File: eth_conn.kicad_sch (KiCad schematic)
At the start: 36 parts, among them T1 H1102NLT, U27 ESDS304DBVR, U3 CD-HD01, U4 CD-HD01

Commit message: did a bit of placement
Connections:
- net MDI.RX-: now also U27.3; no longer U27.5
- net MDI.TX+: now also U27.1; no longer U27.3
- net MDI.TX-: now also U27.5; no longer U27.1

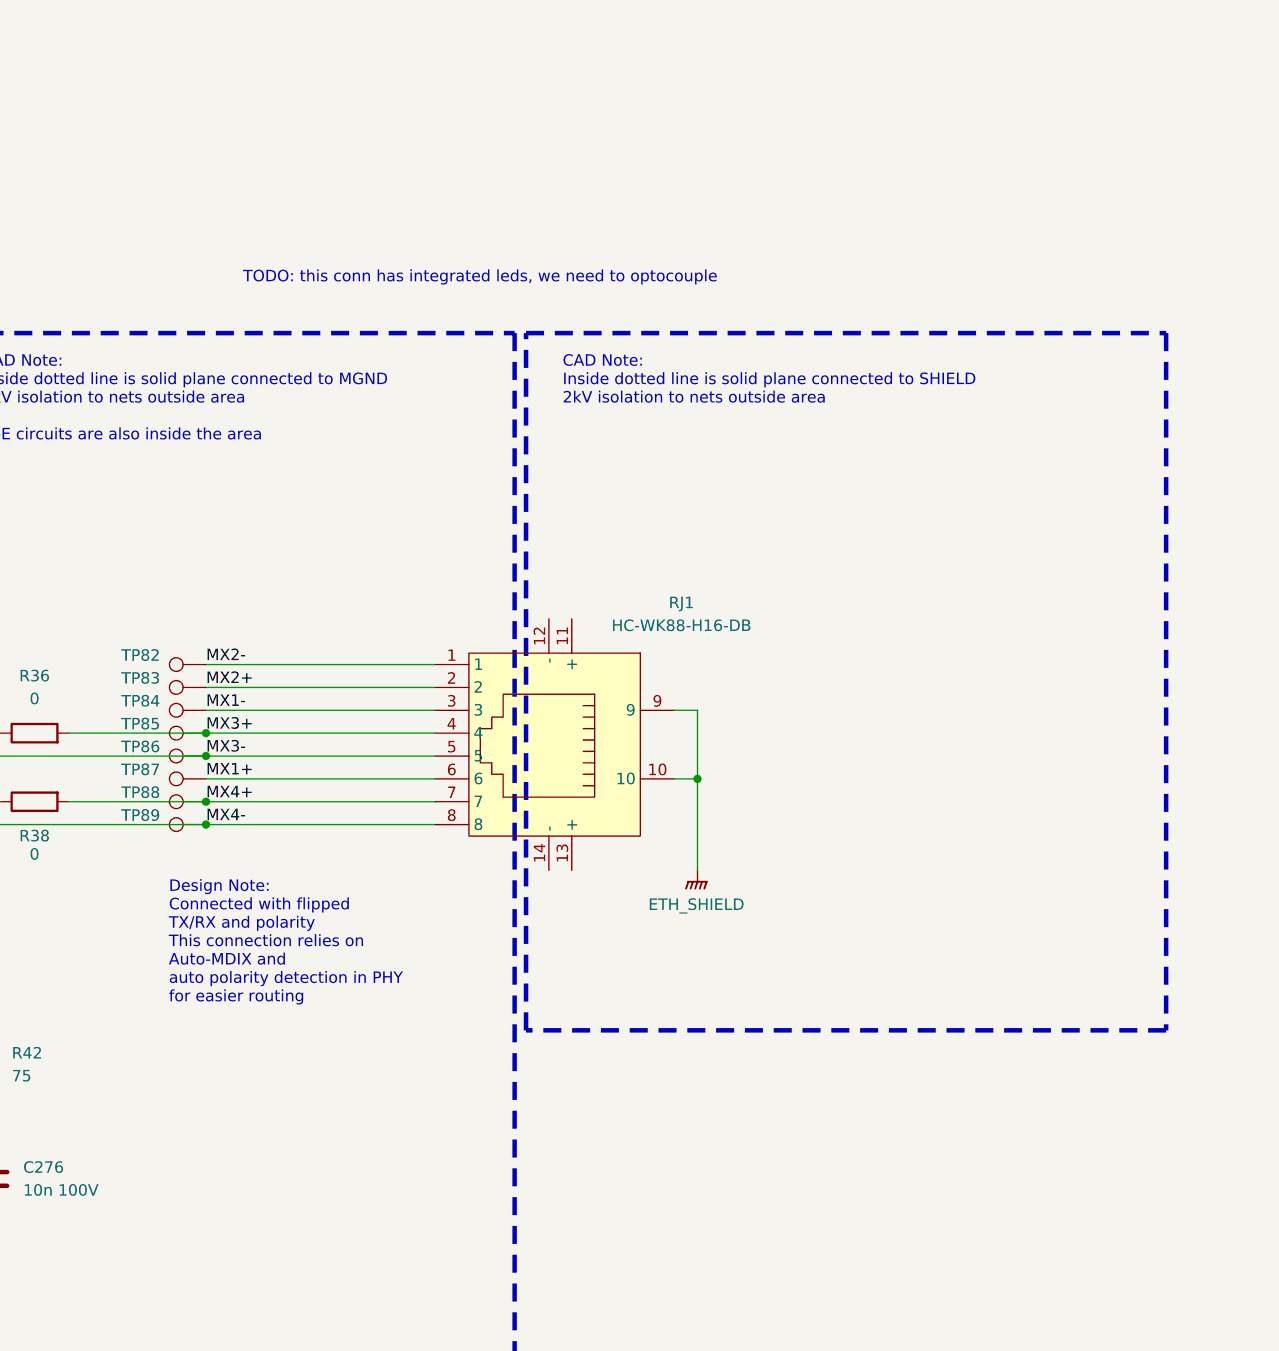
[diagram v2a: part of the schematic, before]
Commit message: cleaned up the schematic review and cleared ERC
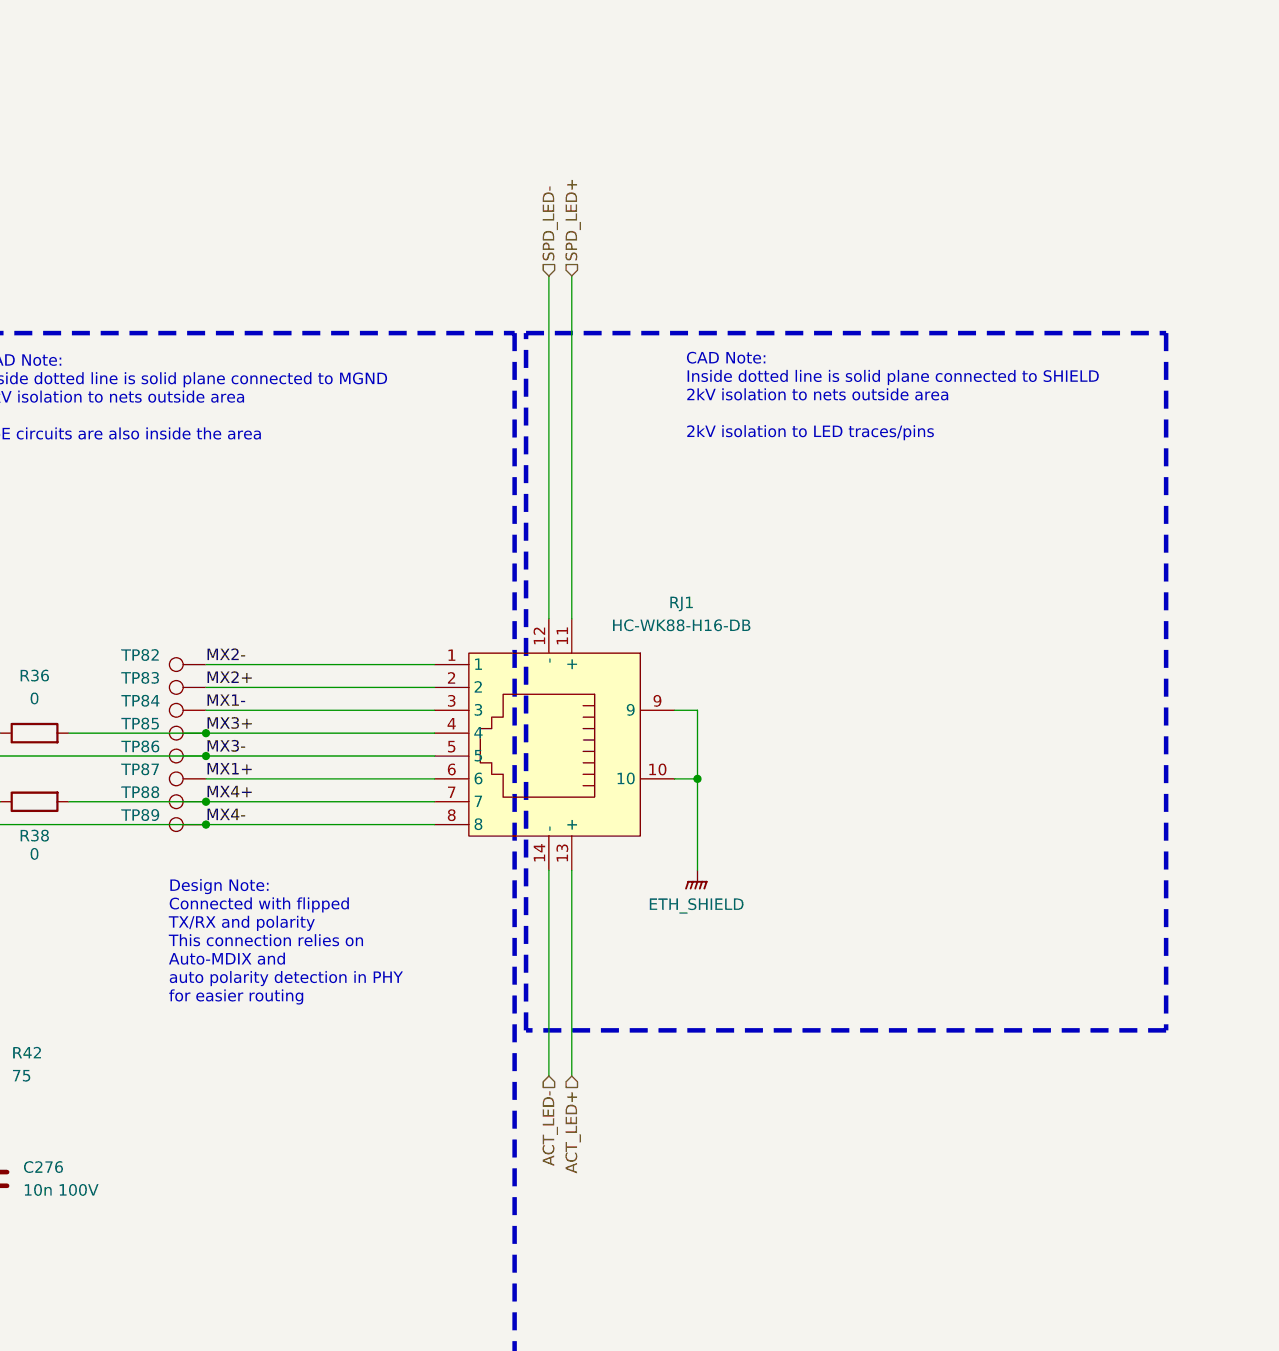
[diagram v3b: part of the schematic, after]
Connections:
- net SPD_LED+: now reaches RJ1.11 (+)
- net SPD_LED-: now reaches RJ1.12 (-)
- net ACT_LED+: now reaches RJ1.13 (+)
- net ACT_LED-: now reaches RJ1.14 (-)
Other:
- note added: "CAD Note: Inside dotted line is solid plane connected to SHIELD 2kV isolation to nets outside area 2kV isolation to LED traces/pins"
- note removed: "CAD Note: Inside dotted line is solid plane connected to SHIELD 2kV isolation to nets outside area"
- note removed: "TODO: this conn has integrated leds, we need to optocouple"
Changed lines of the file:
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@@
 		)
 	)
-	(text "TODO: this conn has integrated leds, we need to optocouple"
-		(exclude_from_sim no)
-		(at 328.93 89.154 0)
-		(effects
-			(font
-				(size 1.27 1.27)
-			)
-		)
-	)
 	(text "DNM"
 		(exclude_from_sim no)
@@
 		)
 	)
-	(text "CAD Note:\nInside dotted line is solid plane connected to SHIELD\n2kV isolation to nets outside area\n"
+	(text "CAD Note:\nInside dotted line is solid plane connected to SHIELD\n2kV isolation to nets outside area\n\n2kV isolation to LED traces/pins"
 		(exclude_from_sim no)
-		(at 338.074 97.79 0)
+		(at 351.79 97.536 0)
 		(effects
 			(font
@@
 	(wire
 		(pts
+			(xy 336.55 88.9) (xy 336.55 127)
+		)
+		(stroke
+			(width 0)
+			(type default)
+		)
+	)
+	(wire
+		(pts
 			(xy 40.64 166.37) (xy 58.42 166.37)
 		)
@@
 	(wire
 		(pts
+			(xy 336.55 154.94) (xy 336.55 177.8)
+		)
+		(stroke
+			(width 0)
+			(type default)
+		)
+	)
+	(wire
+		(pts
 			(xy 93.98 140.97) (xy 93.98 144.78)
 		)
@@
 	(wire
 		(pts
+			(xy 339.09 154.94) (xy 339.09 177.8)
+		)
+		(stroke
+			(width 0)
+			(type default)
+		)
+	)
+	(wire
+		(pts
 			(xy 243.84 207.01) (xy 243.84 208.28)
 		)
@@
 	(wire
 		(pts
+			(xy 339.09 88.9) (xy 339.09 127)
+		)
+		(stroke
+			(width 0)
+			(type default)
+		)
+	)
+	(wire
+		(pts
 			(xy 274.32 147.32) (xy 275.59 147.32)
 		)
@@
 		)
 	)
+	(hierarchical_label "SPD_LED-"
+		(shape input)
+		(at 336.55 88.9 90)
+		(effects
+			(font
+				(size 1.27 1.27)
+			)
+			(justify left)
+		)
+	)
 	(hierarchical_label "POE_V+"
 		(shape output)
@@
 		)
 	)
+	(hierarchical_label "SPD_LED+"
+		(shape input)
+		(at 339.09 88.9 90)
+		(effects
+			(font
+				(size 1.27 1.27)
+			)
+			(justify left)
+		)
+	)
+	(hierarchical_label "ACT_LED-"
+		(shape input)
+		(at 336.55 177.8 270)
+		(effects
+			(font
+				(size 1.27 1.27)
+			)
+			(justify right)
+		)
+	)
 	(hierarchical_label "POE_V-"
 		(shape output)
@@
 		)
 	)
+	(hierarchical_label "ACT_LED+"
+		(shape input)
+		(at 339.09 177.8 270)
+		(effects
+			(font
+				(size 1.27 1.27)
+			)
+			(justify right)
+		)
+	)
 	(rule_area
 		(exclude_from_sim no)
@@
 			)
 		)
-		(property "Datasheet" "https://wmsc.lcsc.com/wmsc/upload/file/pdf/v2/lcsc/2410010331_Pulse-Elec-H1102NLT_C18584.pdf"
+		(property "Datasheet" "https://lcsc.com/product-detail/RJ45-Transformer_H1102NLT_C18584.html"
 			(at 163.83 120.65 0)
 			(hide yes)
@@
 			)
 		)
-		(property "Datasheet" "https://datasheet.lcsc.com/lcsc/2303020130_Texas-Instruments-ESDS304DBVR_C1847869.pdf"
+		(property "Datasheet" "https://www.ti.com/lit/gpn/esds304"
 			(at 56.896 124.968 0)
 			(hide yes)
